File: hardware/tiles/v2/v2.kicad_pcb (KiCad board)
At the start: 2 copper layers, 50 x 50 mm, 24 parts, among them J1 Conn_01x05_Pin, J2 Conn_01x05_Pin, J3 Conn_01x05_Pin, J4 Conn_01x05_Pin, J5 Conn_01x05_Pin, J6 Conn_01x05_Pin, J7 Conn_01x05_Pin, J8 Conn_01x05_Pin, J9 Conn_01x06_Pin, SW1 SW_DIP_x01, U1 ATmega328P-A, U2 DRV5055A2xDBZxQ1, Y2 Crystal_GND24

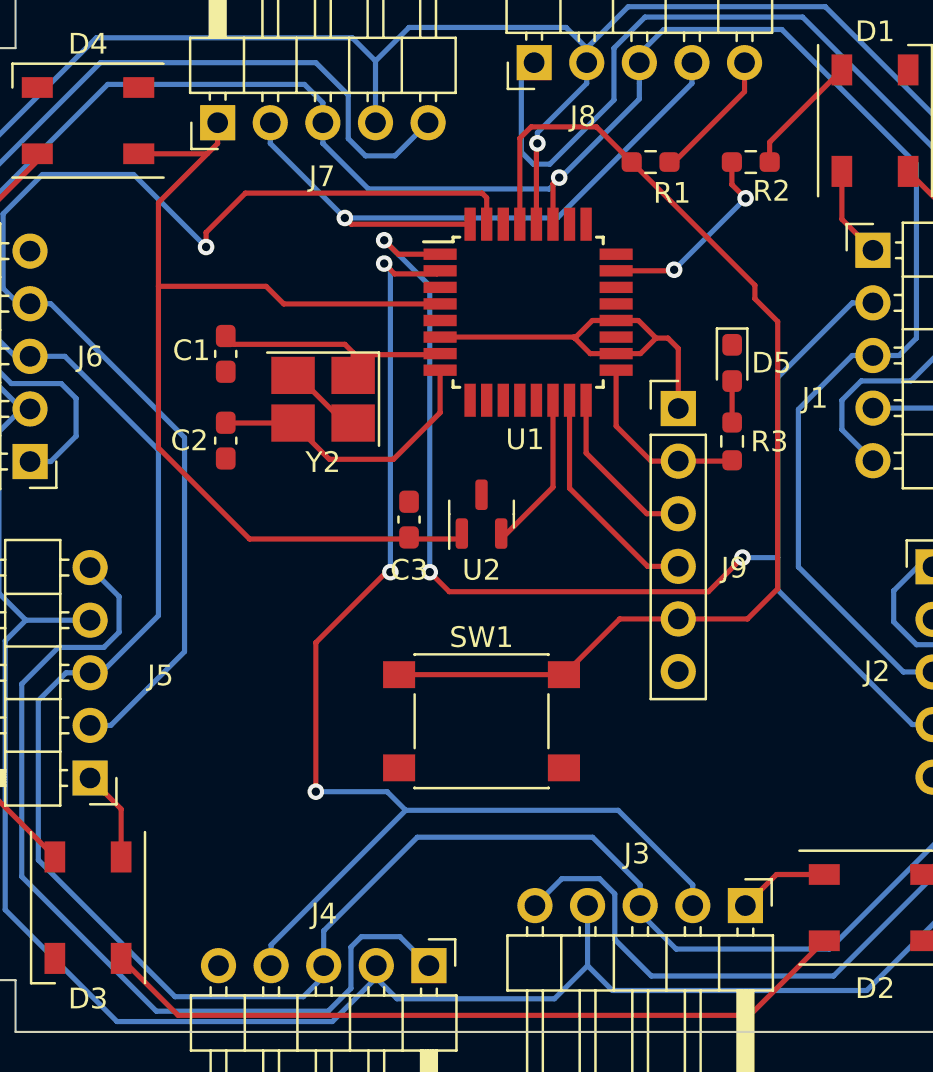
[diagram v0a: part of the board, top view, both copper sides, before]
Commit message: Updating PCB with Capacitive touch and Color sensor
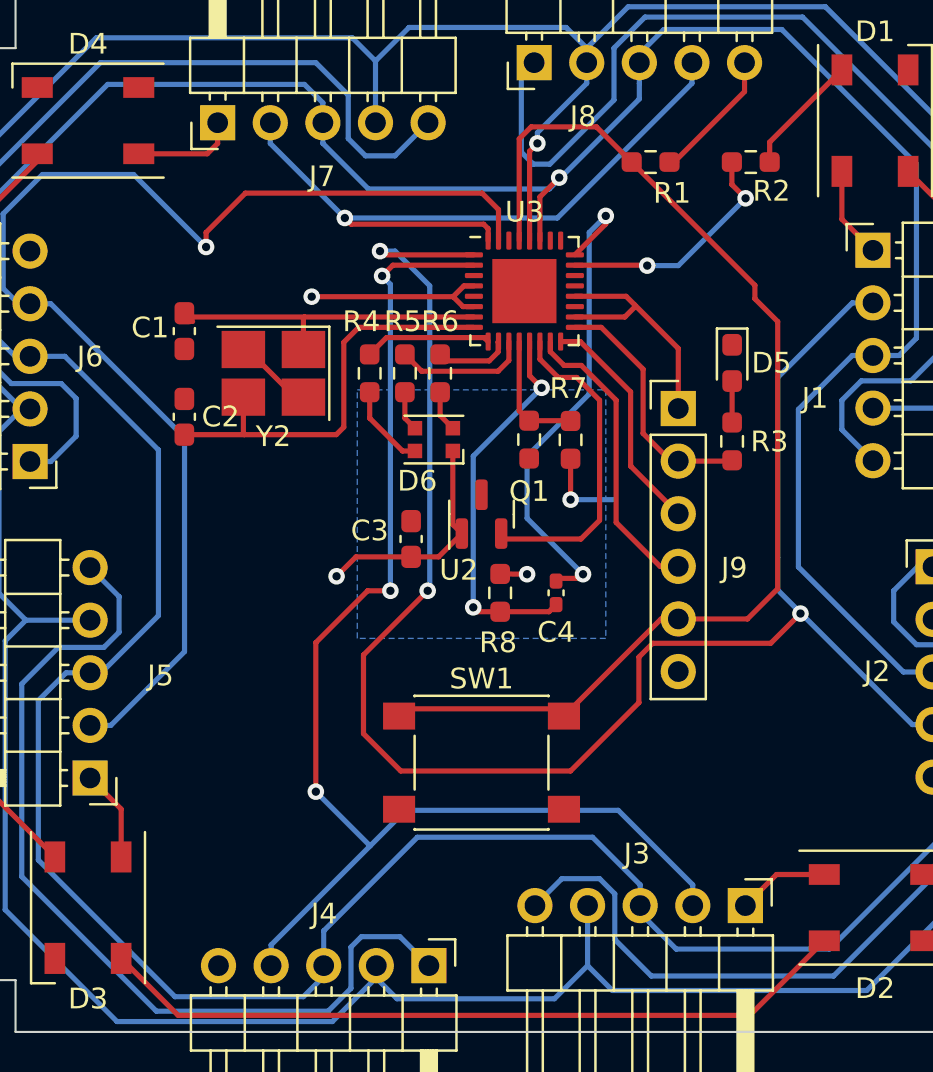
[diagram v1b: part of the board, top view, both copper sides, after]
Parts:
- removed U1: ATmega328P-A, Package_QFP:TQFP-32_7x7mm_P0.8mm
- added C4: C, Capacitor_SMD:C_0402_1005Metric_Pad0.74x0.62mm_HandSolder, F.Cu at (103.6, 103.8)
- added D6: LED_ARGB, LED_SMD:LED_WS2812B-2020_PLCC4_2.0x2.0mm, F.Cu at (97.7, 96.4)
- added Q1: Q_Photo_NPN_EC, Resistor_SMD:R_0603_1608Metric_Pad0.98x0.95mm_HandSolder, F.Cu at (102.3, 96.4)
- added R4: R, Resistor_SMD:R_0603_1608Metric_Pad0.98x0.95mm_HandSolder, F.Cu at (94.6, 93.2)
- added R5: R, Resistor_SMD:R_0603_1608Metric_Pad0.98x0.95mm_HandSolder, F.Cu at (96.3, 93.2)
- added R6: R, Resistor_SMD:R_0603_1608Metric_Pad0.98x0.95mm_HandSolder, F.Cu at (98.0, 93.2)
- added R7: R, Resistor_SMD:R_0603_1608Metric_Pad0.98x0.95mm_HandSolder, F.Cu at (104.3, 96.4)
- added R8: R, Resistor_SMD:R_0603_1608Metric_Pad0.98x0.95mm_HandSolder, F.Cu at (100.9, 103.8)
- added U3: ATmega328-M, Package_DFN_QFN:QFN-32-1EP_5x5mm_P0.5mm_EP3.1x3.1mm, F.Cu at (102.1, 89.2)
- moved Y2 2.71 mm to (90.0, 93.2)
- moved C2 2.31 mm to (85.7, 95.3), turned to 90 degrees
- moved C1 2.28 mm to (85.7, 91.2)
- moved SW1 2.00 mm to (100.0, 112.0)
- moved C3 0.94 mm to (96.6, 101.2)
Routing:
- net +5V: track 90.2 -> 61.3 mm, vias 0 -> 3
- net /TOUCH_SNS: track 0.00 -> 24.1 mm, vias 0 -> 2
- net /DETEC0: track 64.3 -> 83.5 mm
- net /TOUCH_SNSK: track 0.00 -> 18.8 mm, vias 0 -> 2
- net /MAG: track 7.74 -> 15.5 mm
- net /EMIT1: track 0.00 -> 6.48 mm
- net Net-(U3-XTAL2/PB7): track 14.1 -> 20.4 mm
- net /EMIT0: track 0.00 -> 6.14 mm
- net /COLOR_SENSOR: track 0.00 -> 6.02 mm
- net Net-(U3-XTAL1/PB6): track 11.8 -> 16.2 mm
- net Net-(D6-BK): track 0.00 -> 4.09 mm
- net /EMIT2: track 0.00 -> 3.62 mm
- net /MOSI: track 11.6 -> 14.9 mm
- net /SCK: track 9.52 -> 12.6 mm
- net /MISO: track 8.71 -> 11.3 mm
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- added copper zone on B.Cu, net /TOUCH_ELECTRODE

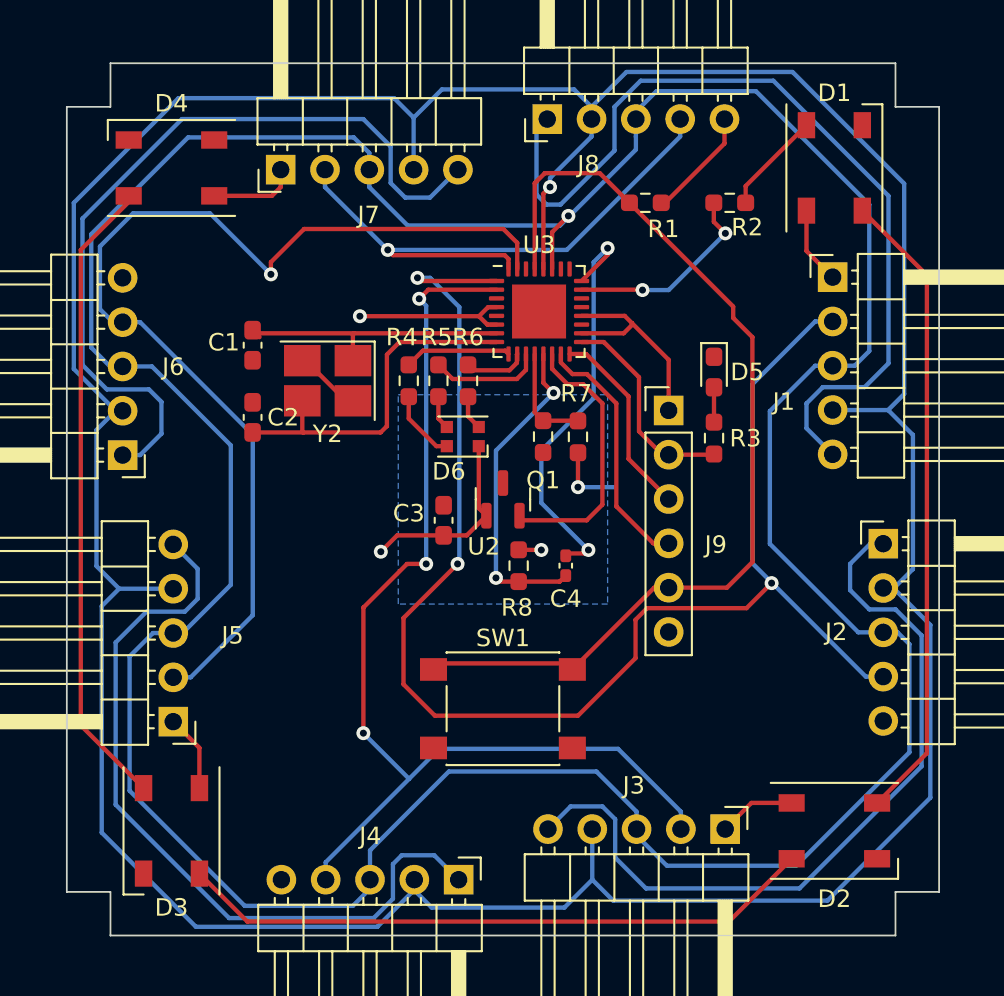
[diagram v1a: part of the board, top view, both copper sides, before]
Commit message: Last atmega238 update
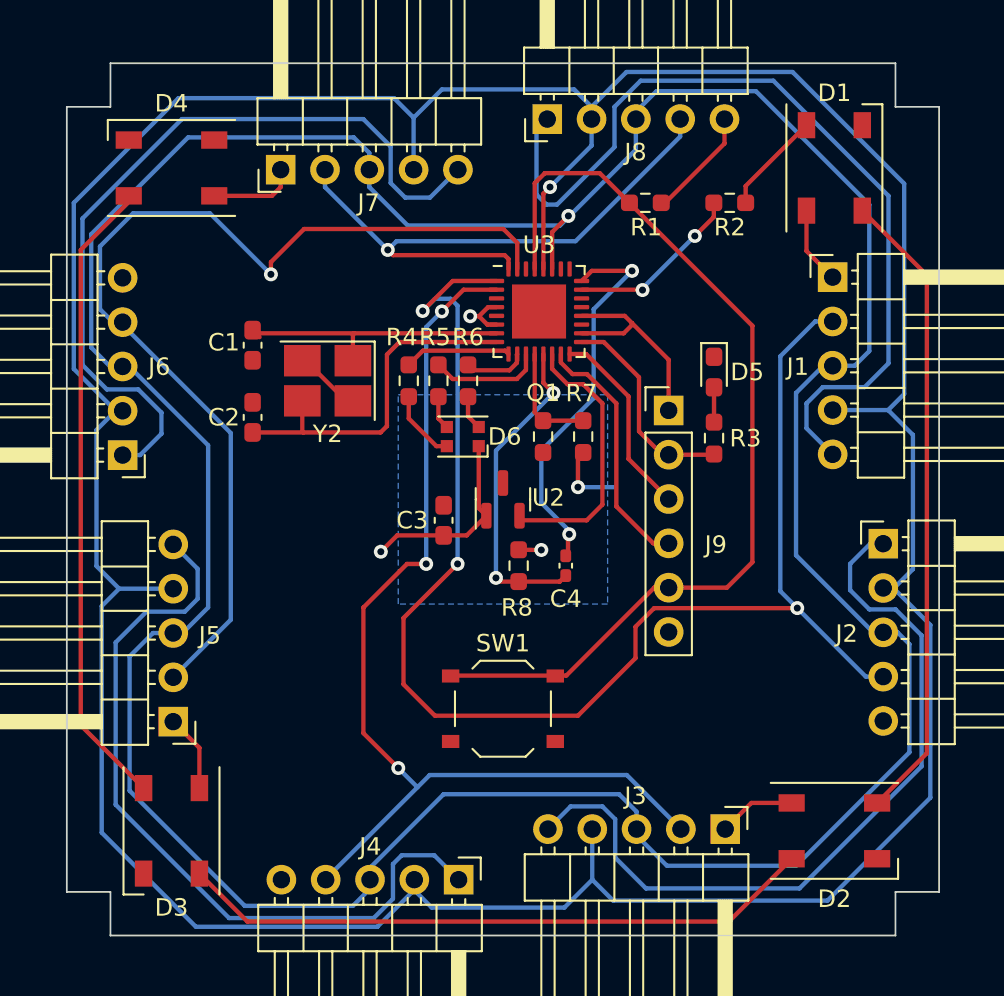
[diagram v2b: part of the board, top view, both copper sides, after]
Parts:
- SW1: footprint Button_Switch_SMD:SW_SPST_PTS645 -> Button_Switch_SMD:SW_Push_1P1T_XKB_TS-1187A
- moved R7 0.30 mm to (104.6, 96.4)
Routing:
- net +5V: track 61.3 -> 55.1 mm
- net /SDA: track 198.1 -> 192.6 mm
- net /DETEC1: track 62.1 -> 58.9 mm
- net /DETEC2: track 61.2 -> 58.9 mm
- net /TOUCH_SNS: track 24.1 -> 22.4 mm
- net /DIN: track 11.6 -> 10.2 mm
- net /DETEC0: track 83.5 -> 82.5 mm

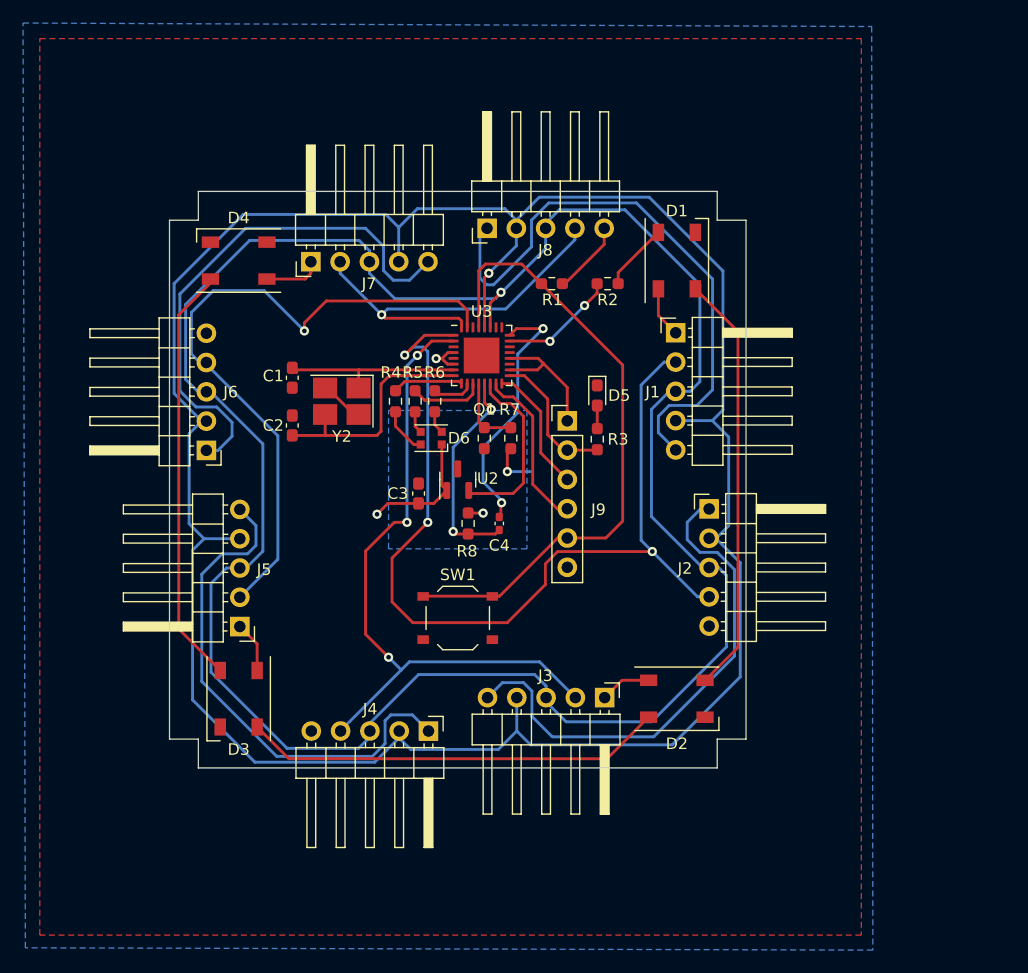
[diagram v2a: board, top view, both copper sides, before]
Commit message: Updating pcb to support U-shaped pin connection, adding AREF decoupler
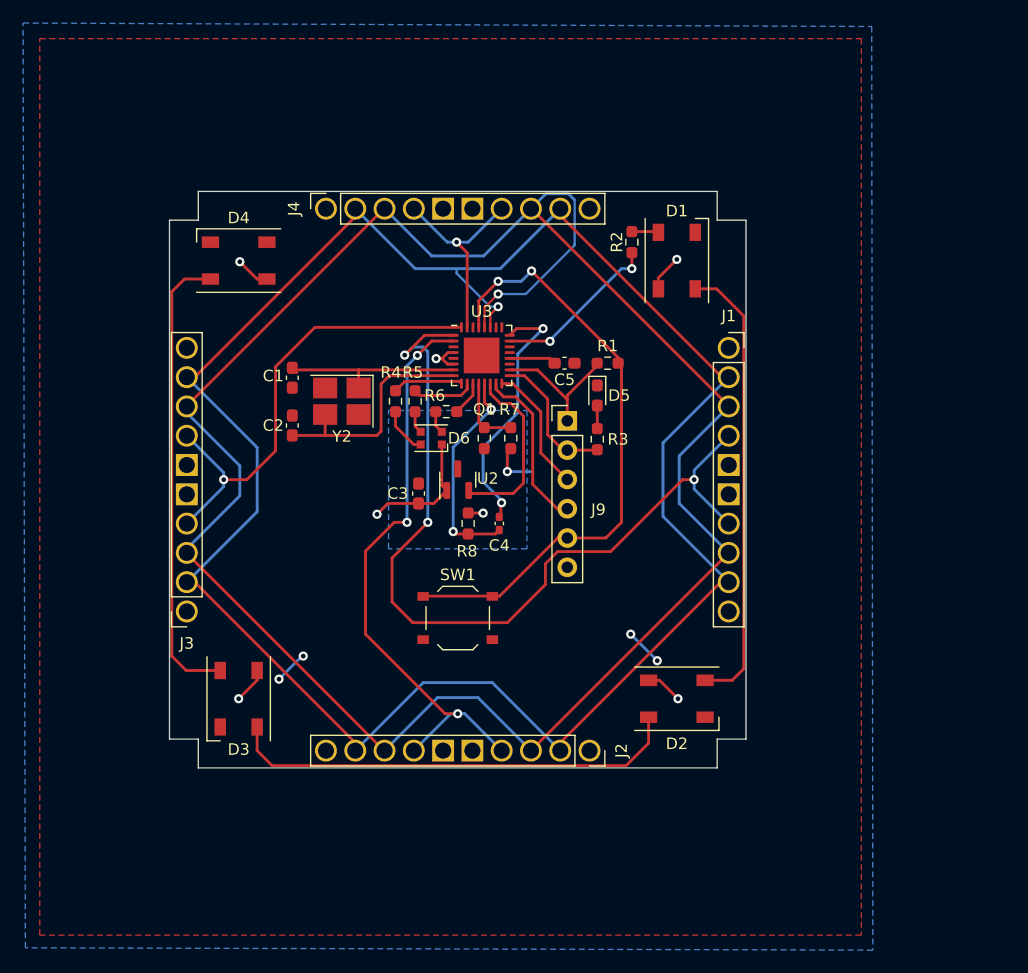
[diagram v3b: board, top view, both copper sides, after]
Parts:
- removed J5, J6, J7, J8: Conn_01x05_Pin, Connector_PinHeader_2.54mm:PinHeader_1x05_P2.54mm_Horizontal
- added C5: 100nf, Capacitor_SMD:C_0603_1608Metric_Pad1.08x0.95mm_HandSolder, F.Cu at (109.3, 89.9)
- C1, C2: value 12pf -> 22pf
- C4: value C -> 22nf
- J1, J2, J3, J4: value Conn_01x05_Pin -> Conn_01x10_Socket; footprint Connector_PinHeader_2.54mm:PinHeader_1x05_P2.54mm_Horizontal -> Connector_PinSocket_2.54mm:PinSocket_1x10_P2.54mm_Vertical
- R2: value R -> 300Ohm
- R4, R5: value R -> 90Ohm
- R6: value R -> 150Ohm
- R7: value R -> 10kOhm
- R8: value R -> 1kOhm
- Y2: value Crystal_GND24 -> Crystal
- moved J4 46.2 mm to (88.6, 76.5), turned to 90 degrees
- moved J3 37.0 mm to (76.5, 111.4), turned to 180 degrees
- moved J2 23.4 mm to (111.4, 123.5), turned to -90 degrees
- moved R1 8.43 mm to (113.0, 89.9), turned to 180 degrees
- moved J1 4.78 mm to (123.5, 88.6)
- moved R2 4.17 mm to (115.1, 79.4), turned to 90 degrees
- moved R6 1.35 mm to (99.0, 94.1), turned to 180 degrees
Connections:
- J1 pad 2: /DETEC0 -> /SDA
- J1 pad 3: /SDA -> /SCL
- J1 pad 4: /SCL -> /DETEC0
- J2 pad 1: GND -> +5V
- J2 pad 2: /SCL -> /SDA
- J2 pad 3: /SDA -> /SCL
- J2 pad 4: /DETEC0 -> /DETEC1
- J2 pad 5: +5V -> GND
- J3 pad 2: /DETEC1 -> /SDA
- J3 pad 3: /SDA -> /SCL
- J3 pad 4: /SCL -> /DETEC2
- J4 pad 1: GND -> +5V
- J4 pad 2: /SCL -> /SDA
- J4 pad 3: /SDA -> /SCL
- J4 pad 4: /DETEC1 -> /DETEC3
- J4 pad 5: +5V -> GND
- U3 pad 10: /EMIT2 -> /EMIT1
- U3 pad 11: /EMIT1 -> /EMIT2
- U3 pad 20: +5V -> Net-(U3-AREF)
- U3 pad 31: /DETEC2 -> /DETEC3
- U3 pad 32: /DETEC3 -> /DETEC2
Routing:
- net GND: track 189.4 -> 6.32 mm, vias 0 -> 4
- net /SCL: track 209.0 -> 184.0 mm
- net /DETEC2: track 58.9 -> 40.6 mm
- net /DETEC3: track 34.3 -> 17.8 mm
- net +5V: track 55.1 -> 42.9 mm, vias 3 -> 7
- net /SDA: track 192.6 -> 181.6 mm
- net /DETEC0: track 82.5 -> 73.6 mm
- net /DETEC1: track 58.9 -> 51.5 mm
- net /DIN: track 10.2 -> 14.7 mm
- net Net-(U3-AREF): track 0.00 -> 4.07 mm
- net Net-(D1-DIN): track 5.89 -> 2.33 mm
- net Net-(D3-DOUT): track 36.6 -> 40.1 mm
- net Net-(D2-DOUT): track 36.6 -> 39.6 mm
- net Net-(D1-DOUT): track 36.7 -> 39.5 mm
- net /RESET: track 55.6 -> 53.3 mm, vias 0 -> 2
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
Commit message: Quick save
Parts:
- removed C5: 100nf, Capacitor_SMD:C_0603_1608Metric_Pad1.08x0.95mm_HandSolder
- removed D6: LED_ARGB, LED_SMD:LED_WS2812B-2020_PLCC4_2.0x2.0mm
- removed J9: Conn_01x06_Pin, Connector_PinHeader_2.54mm:PinHeader_1x06_P2.54mm_Vertical
- removed R4, R5: 90Ohm, Resistor_SMD:R_0603_1608Metric_Pad0.98x0.95mm_HandSolder
- removed R6: 150Ohm, Resistor_SMD:R_0603_1608Metric_Pad0.98x0.95mm_HandSolder
- removed R8: 1kOhm, Resistor_SMD:R_0603_1608Metric_Pad0.98x0.95mm_HandSolder
- removed Y2: Crystal, Crystal:Crystal_SMD_3225-4Pin_3.2x2.5mm_HandSoldering
- added C6: 1 uF, Capacitor_SMD:C_0603_1608Metric_Pad1.08x0.95mm_HandSolder, F.Cu at (133.9, 101.8)
- added D7: SK6812, LED_SMD:LED_SK6812_PLCC4_5.0x5.0mm_P3.2mm, F.Cu at (97.5, 105.0)
- added J5: Conn_01x05_Socket, Connector_PinSocket_2.54mm:PinSocket_1x05_P2.54mm_Vertical, F.Cu at (129.5, 96.2)
- added R7: 10kOhm, Resistor_SMD:R_0603_1608Metric_Pad0.98x0.95mm_HandSolder, F.Cu at (141.3, 95.6)
- added SW2: SW_DIP_x01, Button_Switch_SMD:SW_Push_1P1T_XKB_TS-1187A, F.Cu at (105.0, 115.9)
- added U1: ESP32-S3-MINI-1, custom:ESP32-S3-MINI-1U, F.Cu at (100.0, 88.0)
- C1: value 22pf -> 1 u; footprint Capacitor_SMD:C_0603_1608Metric_Pad1.08x0.95mm_HandSolder -> Capacitor_SMD:C_0603_1608Metric
- C2: value 22pf -> 1 uF
- C4: value 22nf -> 0.1 u; footprint Capacitor_SMD:C_0402_1005Metric_Pad0.74x0.62mm_HandSolder -> Capacitor_SMD:C_0603_1608Metric
- R1: value 10kOhm -> 10k
- U3: value ATmega328-M -> AP7362A-33SP-13; footprint Package_DFN_QFN:QFN-32-1EP_5x5mm_P0.5mm_EP3.1x3.1mm -> custom:SOIC127P600X163-9N
- moved C2 57.2 mm to (140.9, 80.6), turned to 0 degrees
- moved U3 42.0 mm to (144.0, 91.1)
- moved R2 33.0 mm to (87.7, 97.8), turned to 180 degrees
- moved R3 31.8 mm to (140.9, 83.1), turned to 0 degrees
- moved C1 22.6 mm to (97.4, 110.5), turned to 180 degrees
- moved C4 10.3 mm to (97.4, 112.0), turned to 0 degrees
- moved D5 9.44 mm to (112.3, 102.1)
- moved Q1 8.60 mm to (102.5, 105.0)
- moved R10 8.60 mm to (104.6, 105.0)
- moved R1 8.25 mm to (114.1, 98.1)
- moved SW1 6.46 mm to (94.8, 115.9)
- moved C3 1.33 mm to (97.4, 100.1)
- renumbered R7 to R10
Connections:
- C1 pad 1: Net-(U3-XTAL1/PB6) -> /EN
- C2 pad 1: Net-(U3-XTAL2/PB7) -> +5V
- C4 pad 1: /TOUCH_SNSK -> /EN
- C4 pad 2: /TOUCH_SNS -> GND
- R1 pad 1: /RESET -> +3V3
- R1 pad 2: +5V -> /EN
- R10 pad 1: +5V -> +3V3
- R2 pad 2: Net-(D1-DIN) -> Net-(D7-DIN)
- R3 pad 1: /SCK -> /RX
- SW1 pad 1: /RESET -> /EN
- U3 pad 1: /DETEC0 -> GND
- U3 pad 2: /DETEC1 -> +5V
- U3 pad 3: GND -> +5V
- U3 pad 5: GND -> +3V3
- U3 pad 6: +5V -> +3V3
- U3 pad 7: Net-(U3-XTAL1/PB6) -> +3V3
- U3 pad 8: Net-(U3-XTAL2/PB7) -> unconnected-(U3-NC-Pad8)
- U3 pad 9: /EMIT0 -> (no net)
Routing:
- net /DETEC0: track 73.6 -> 0.00 mm, vias 3 -> 0
- net /RESET: track 53.3 -> 0.00 mm, vias 2 -> 0
- net /DETEC1: track 51.5 -> 0.00 mm, vias 3 -> 0
- net /DETEC2: track 40.6 -> 0.00 mm, vias 1 -> 0
- net Net-(D3-DOUT): track 40.1 -> 0.00 mm
- net Net-(D2-DOUT): track 39.6 -> 0.00 mm
- net Net-(D1-DOUT): track 39.5 -> 0.00 mm
- net +5V: track 42.9 -> 6.98 mm, vias 7 -> 4
- net /TOUCH_SNS: track 22.4 -> 0.00 mm, vias 2 -> 0
- net Net-(U3-XTAL2/PB7): track 20.4 -> 0.00 mm
- net /TOUCH_SNSK: track 18.8 -> 0.00 mm, vias 2 -> 0
- net /DETEC3: track 17.8 -> 0.00 mm, vias 1 -> 0
- net Net-(U3-XTAL1/PB6): track 16.2 -> 0.00 mm
- net /MAG: track 15.5 -> 0.00 mm
- net /MOSI: track 15.0 -> 0.00 mm
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- added copper zone on B.Cu, net /TOUCH
- removed copper zone on B.Cu, net /TOUCH_ELECTRODE
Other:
- copper layers 2 -> 4
